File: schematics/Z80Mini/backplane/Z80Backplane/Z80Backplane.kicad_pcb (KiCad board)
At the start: 2 copper layers, 151.1 x 94 mm, 28 parts, among them J1 CPU-IO BOARD, J2 GRAPHICS_SOUND_CARD, J3 EXPANSION_1, J4 EXPANSION_2, J5 Screw_Terminal_01x02, Q1 BC337, SW1 SW_SPDT, U1 L7805, U2 74LS138, U3 74LS139

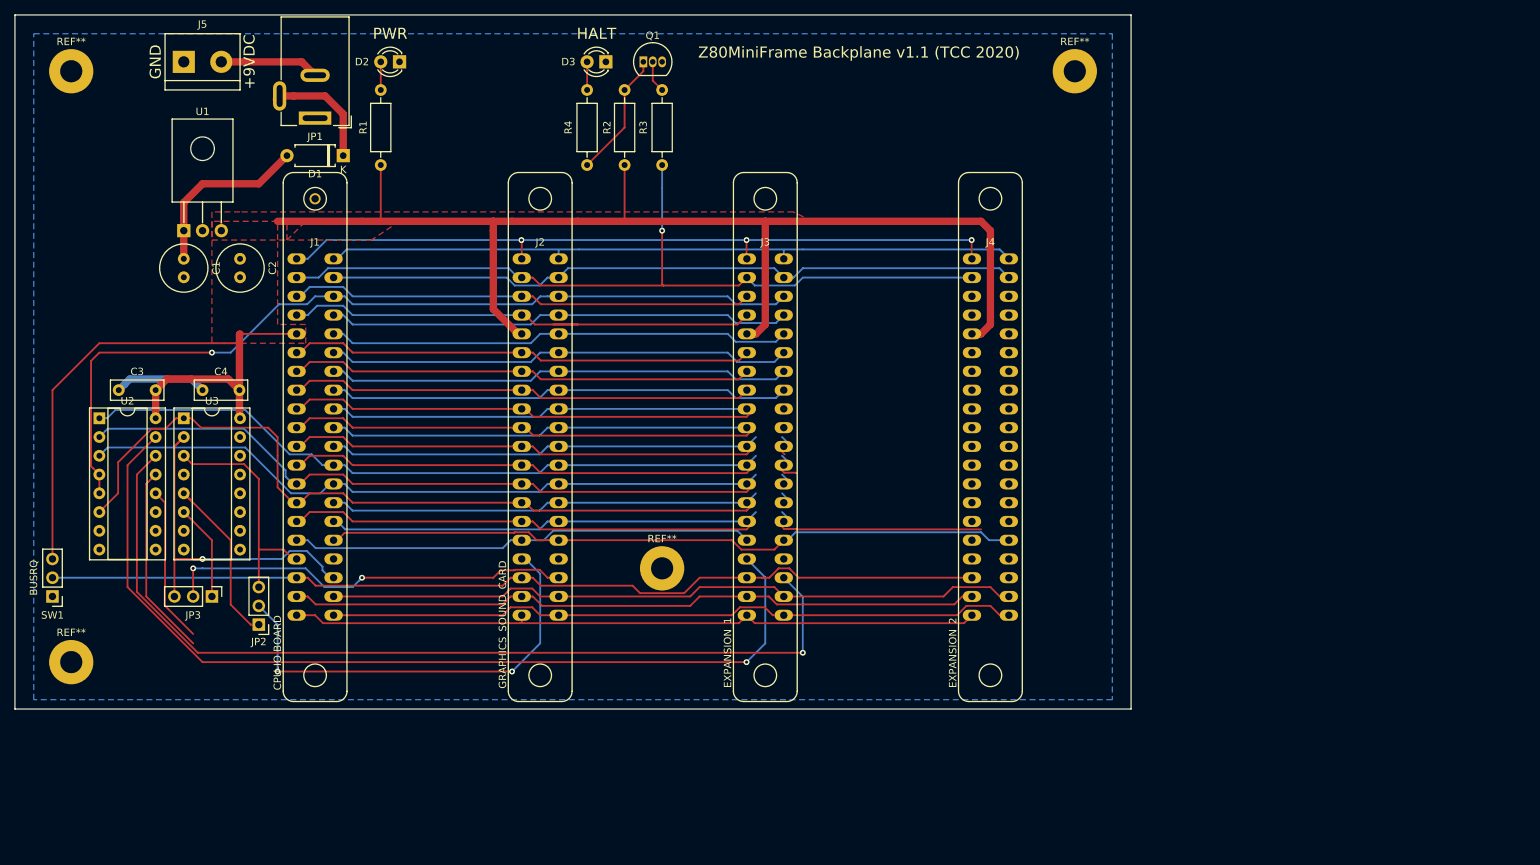
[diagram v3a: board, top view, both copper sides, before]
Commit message: Latest code changes and modified Makefile to support burn to EPROM Emulator
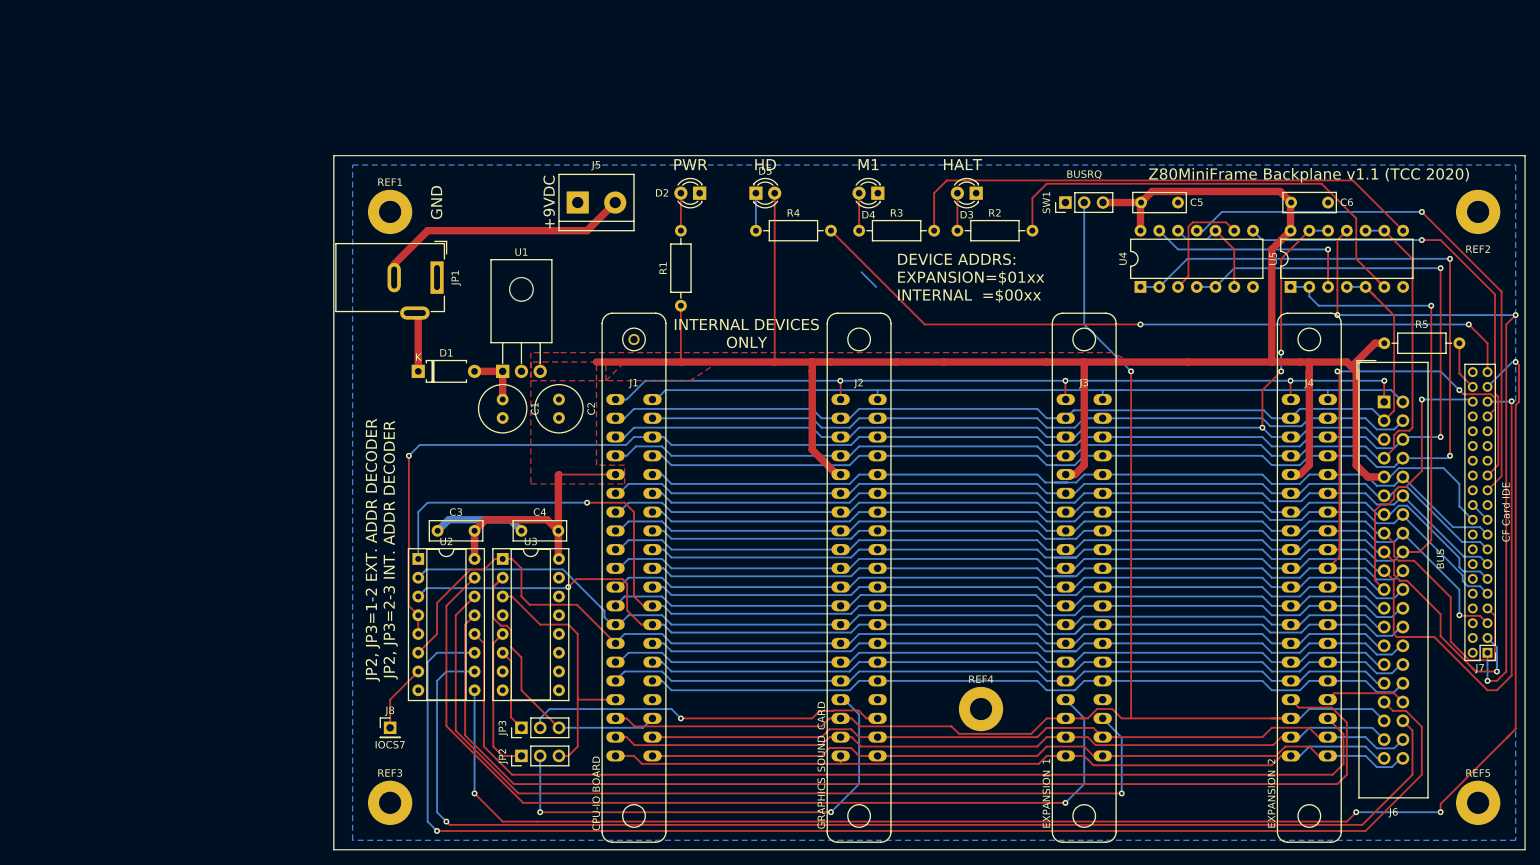
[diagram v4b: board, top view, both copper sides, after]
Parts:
- removed Q1: BC337, Package_TO_SOT_THT:TO-92_Inline
- added C5: 100nF, Capacitor_THT:C_Disc_D7.0mm_W2.5mm_P5.00mm, F.Cu at (184.2, 54.6)
- added C6: 100nF, Capacitor_THT:C_Disc_D7.0mm_W2.5mm_P5.00mm, F.Cu at (204.5, 54.6)
- added D4: LED_M1, LED_THT:LED_D3.0mm, F.Cu at (143.5, 53.3)
- added D5: LED_CF_ACTIV, LED_THT:LED_D3.0mm, F.Cu at (127.0, 53.3)
- added J6: BUS, Connector_IDC:IDC-Header_2x20_P2.54mm_Vertical, F.Cu at (212.1, 81.6)
- added J7: CF Card IDE, Connector_PinHeader_2.00mm:PinHeader_2x20_P2.00mm_Vertical, F.Cu at (226.1, 115.6)
- added J8: IOCS7, Connector_PinHeader_2.54mm:PinHeader_1x01_P2.54mm_Vertical, F.Cu at (77.5, 125.7)
- added R5: 1K, Resistor_THT:R_Axial_DIN0207_L6.3mm_D2.5mm_P10.16mm_Horizontal, F.Cu at (222.2, 73.7)
- added REF5: MountingHole_3mm_Pad, MountingHole:MountingHole_3mm_Pad, F.Cu at (224.8, 135.9)
- added U4: 74HC00, Package_DIP:DIP-14_W7.62mm, F.Cu at (179.1, 66.0)
- added U5: 74HC00, Package_DIP:DIP-14_W7.62mm, F.Cu at (199.4, 66.0)
- R3: value 1K -> 330R
- R4: value 330R -> 1K
- moved SW1 147.2 mm to (168.9, 54.6), turned to 90 degrees
- moved REF2 57.8 mm to (224.8, 55.9)
- moved J5 56.6 mm to (102.9, 54.6)
- moved D3 53.2 mm to (156.8, 53.3)
- moved C3 47.2 mm to (83.9, 99.1)
- moved J4 47.2 mm to (201.9, 105.4)
- moved U2 47.2 mm to (81.3, 102.9)
- moved C2 47.2 mm to (100.3, 81.3)
- moved C4 47.2 mm to (95.2, 99.1)
- moved REF1 47.2 mm to (77.5, 55.9)
- moved U3 47.2 mm to (92.7, 102.9)
- moved C1 47.2 mm to (92.7, 81.3)
- moved J1 47.2 mm to (110.5, 105.4)
- moved J2 47.2 mm to (141.0, 105.4)
- moved REF3 47.2 mm to (77.5, 135.9)
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- renumbered REF** to REF1, REF** to REF2, REF** to REF3, REF** to REF4
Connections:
- net Net-(J2-Pad33) renamed /VDP_SEL1
- net Net-(J2-Pad36) renamed /SND_SEL1
- net Net-(J3-Pad33) renamed /IOCS0
- R2 pad 1: VCC -> Net-(D3-Pad2)
- R2 pad 2: Net-(Q1-Pad1) -> Net-(R2-Pad2)
- R3 pad 2: /HALT -> Net-(R3-Pad2)
- R4 pad 1: Net-(D3-Pad2) -> Net-(D5-Pad1)
- R4 pad 2: Net-(Q1-Pad1) -> Net-(J7-Pad39)
- REF2 pad 2: (no net) -> GND
- REF3 pad 3: (no net) -> GND
- U2 pad 9: Net-(U2-Pad9) -> /IOCS6
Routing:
- net /IOCS6: track 0.00 -> 218.1 mm, vias 0 -> 4
- net Net-(J6-Pad33): track 0.00 -> 179.8 mm, vias 0 -> 1
- net Net-(J6-Pad36): track 0.00 -> 166.8 mm, vias 0 -> 1
- net Net-(J4-Pad33): track 26.0 -> 155.4 mm
- net Net-(J4-Pad36): track 21.2 -> 141.4 mm
- net /RD: track 63.9 -> 183.1 mm, vias 0 -> 2
- net /A0: track 64.4 -> 177.9 mm, vias 0 -> 1
- net /IORQ: track 117.6 -> 226.8 mm, vias 1 -> 3
- net /WR: track 57.3 -> 165.6 mm, vias 0 -> 1
- net /A1: track 57.3 -> 161.2 mm, vias 0 -> 2
- net Net-(J7-Pad39): track 0.00 -> 99.1 mm, vias 0 -> 2
- net /MR: track 0.00 -> 91.7 mm, vias 0 -> 3
- net /A2: track 64.4 -> 145.4 mm, vias 0 -> 1
- net /D5: track 62.9 -> 142.7 mm
- net /M1: track 67.4 -> 146.4 mm
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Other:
- board size 151.1 x 94 mm -> 161.3 x 94 mm
- board text added: "DEVICE ADDRS: EXPANSION=$01xx INTERNAL =$00xx"
- board text added: "HD"
- board text added: "INTERNAL DEVICES ONLY"
- board text added: "JP2, JP3=1-2 EXT. ADDR DECODER JP2, JP3=2-3 INT. ADDR DECODER"
- board text added: "M1"
